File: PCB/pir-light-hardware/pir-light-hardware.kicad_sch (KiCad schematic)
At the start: 41 parts, among them J1 ZH1.5-3, J2 ZH1.5-3, Q1 AON7240, Q2 NPN, Q3 PNP, U1 M74VHC1GT08DFT2G, U2 LMV331IDCKR, U3 AS312

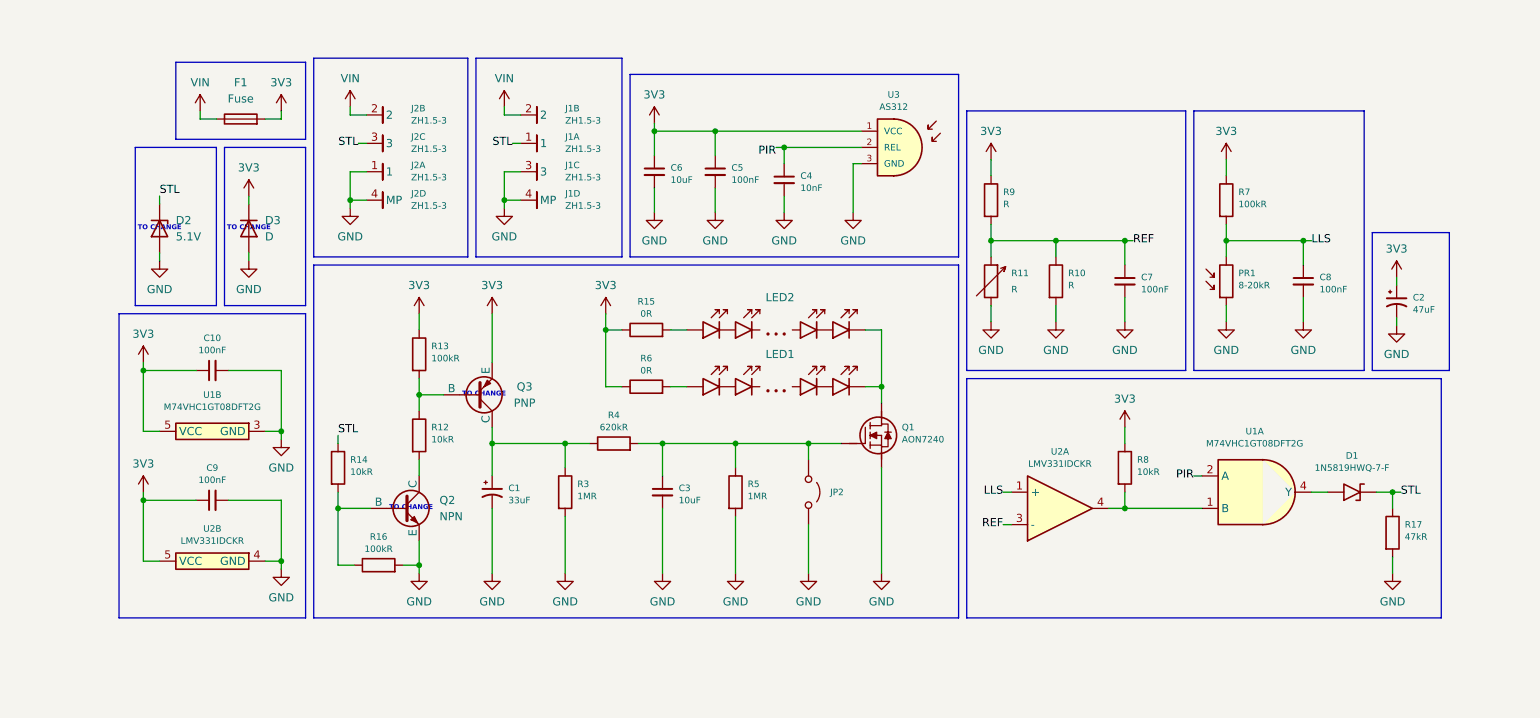
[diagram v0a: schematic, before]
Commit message: feat: sustain motion detection while own light is active
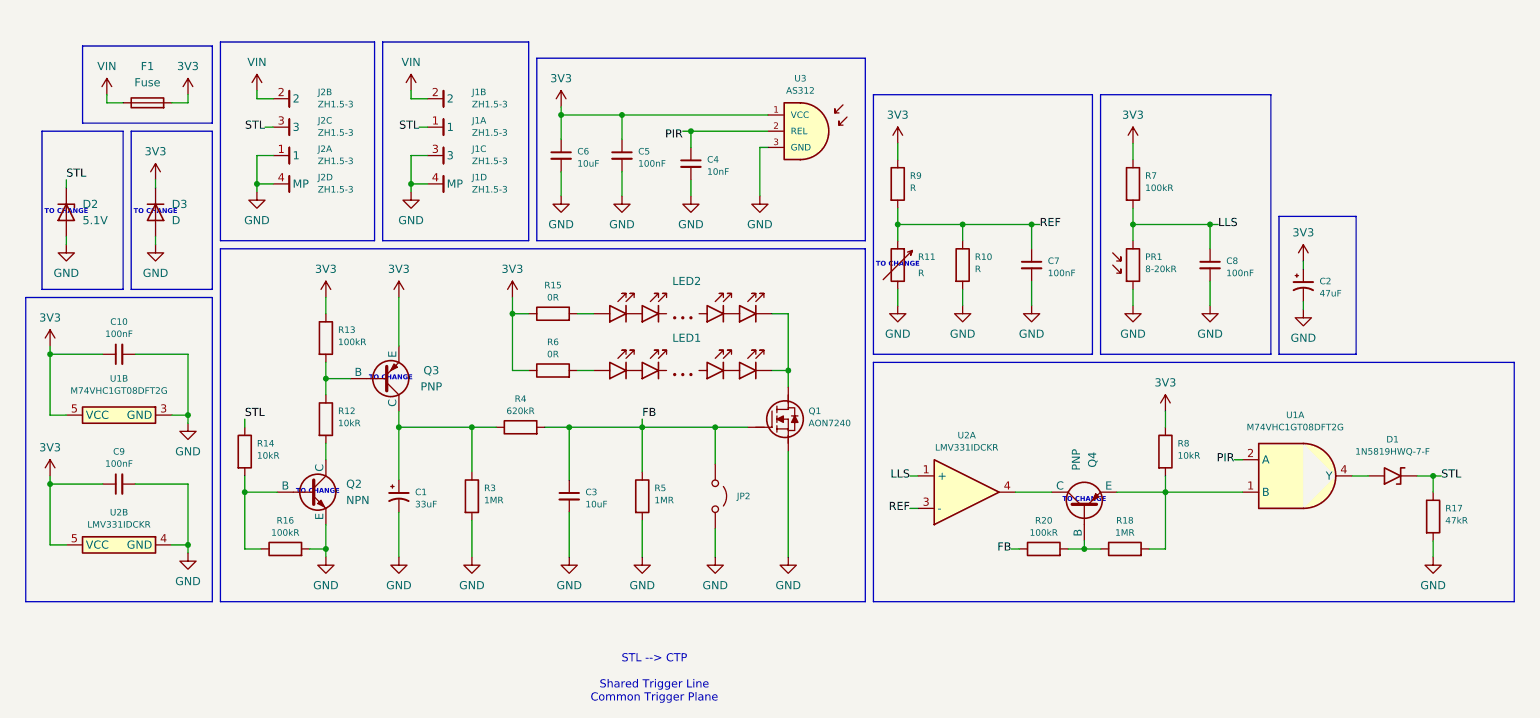
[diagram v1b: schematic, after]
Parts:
- added Q4: PNP, symbol Simulation_SPICE:PNP
- added R18: 1MR, REST:R_0402_1005Metric, symbol REST:R
- added R20: 100kR, REST:R_0402_1005Metric, symbol REST:R
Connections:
- net at R8.2, U1.1 (B): now also Q4.3 (E), R18.2; no longer U2.4
- net FB: now reaches C3.1, JP2.1 (A), Q1.2 (G), R4.2, R5.1
- net FB: now also R20.1
- new net: Q4.1 (C), U2.4
- new net: Q4.2 (B), R18.1, R20.2
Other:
- note added: "STL --> CTP Shared Trigger Line Common Trigger Plane"
- moved on the sheet: C1, C10, C2, C3, C4, C5, C6, C7, C8, C9, D1, D2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

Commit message: docs: update readme
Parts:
- R10: now not fitted
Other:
- note removed: "STL --> CTP Shared Trigger Line Common Trigger Plane"
- company: (none) -> Designed by Marcin Trzmiel
- title: (none) -> PIR motion-controlled light module
- moved on the sheet: C1, C10, C2, C3, C4, C5, C6, C7, C8, C9, D1, D2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
